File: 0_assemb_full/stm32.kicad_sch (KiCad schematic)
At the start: 15 parts, among them J4 Conn_01x02, J5 SPIConn_01x03, U25 STM32F091RCTx

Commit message: Updates to the filter system
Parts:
- added R33, R35, R36: 2k, symbol Device:R_US
- gave numbers to parts that had none: 7
- renumbered J4 to J3, J5 to J4, R62 to R34, U25 to U5
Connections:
- net ADC_BP: now also R35.1; no longer U5.9 (PC1)
- net ADC_HP: now also R36.1; no longer U5.10 (PC2)
- net ADC_LP: now also R33.2; no longer U5.8 (PC0)
- new net: R35.2, U5.9 (PC1)
- new net: R33.1, U5.8 (PC0)
- new net: R36.2, U5.10 (PC2)
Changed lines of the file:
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@@
     (stroke (width 0) (type default) (color 0 0 0 0))
   )
-  (wire (pts (xy 105.41 101.6) (xy 119.38 101.6))
+  (wire (pts (xy 105.41 109.22) (xy 109.22 109.22))
     (stroke (width 0) (type default) (color 0 0 0 0))
   )
@@
     (stroke (width 0) (type default) (color 0 0 0 0))
   )
-  (wire (pts (xy 105.41 96.52) (xy 119.38 96.52))
-    (stroke (width 0) (type default) (color 0 0 0 0))
-  )
   (wire (pts (xy 60.96 93.98) (xy 62.23 93.98))
     (stroke (width 0) (type default) (color 0 0 0 0))
@@
     (stroke (width 0) (type default) (color 0 0 0 0))
   )
+  (wire (pts (xy 109.22 96.52) (xy 119.38 96.52))
+    (stroke (width 0) (type default) (color 0 0 0 0))
+  )
   (wire (pts (xy 185.42 132.08) (xy 195.58 132.08))
     (stroke (width 0) (type default) (color 0 0 0 0))
@@
     (stroke (width 0) (type default) (color 0 0 0 0))
   )
-  (wire (pts (xy 105.41 99.06) (xy 119.38 99.06))
+  (wire (pts (xy 105.41 99.06) (xy 111.76 99.06))
     (stroke (width 0) (type default) (color 0 0 0 0))
   )
@@
   )
   (wire (pts (xy 45.72 73.66) (xy 45.72 74.93))
+    (stroke (width 0) (type default) (color 0 0 0 0))
+  )
+  (wire (pts (xy 109.22 101.6) (xy 119.38 101.6))
+    (stroke (width 0) (type default) (color 0 0 0 0))
+  )
+  (wire (pts (xy 105.41 88.9) (xy 109.22 88.9))
     (stroke (width 0) (type default) (color 0 0 0 0))
   )
@@
     )
   )
-  (global_label "ADC_HP" (shape input) (at 105.41 101.6 180) (fields_autoplaced)
+  (global_label "ADC_HP" (shape input) (at 105.41 109.22 180) (fields_autoplaced)
     (effects (font (size 1.27 1.27)) (justify right))
-    (property "Intersheet References" "${INTERSHEET_REFS}" (id 0) (at 95.8002 101.5206 0)
+    (property "Intersheet References" "${INTERSHEET_REFS}" (id 0) (at 95.8002 109.1406 0)
       (effects (font (size 1.27 1.27)) (justify right) hide)
     )
   )
-  (global_label "ADC_LP" (shape input) (at 105.41 96.52 180) (fields_autoplaced)
+  (global_label "ADC_LP" (shape input) (at 105.41 88.9 180) (fields_autoplaced)
     (effects (font (size 1.27 1.27)) (justify right))
-    (property "Intersheet References" "${INTERSHEET_REFS}" (id 0) (at 96.1026 96.4406 0)
+    (property "Intersheet References" "${INTERSHEET_REFS}" (id 0) (at 96.1026 88.8206 0)
       (effects (font (size 1.27 1.27)) (justify right) hide)
     )
@@
   (symbol (lib_id "Connector_Generic:Conn_01x03") (at 200.66 129.54 0) (unit 1)
     (in_bom yes) (on_board yes) (fields_autoplaced)
-    (property "Reference" "J5" (id 0) (at 203.2 128.2699 0)
+    (property "Reference" "J4" (id 0) (at 203.2 128.2699 0)
       (effects (font (size 1.27 1.27)) (justify left))
     )
@@
   (symbol (lib_id "Device:C") (at 31.75 25.4 0) (unit 1)
     (in_bom yes) (on_board yes) (fields_autoplaced)
-    (property "Reference" "C?" (id 0) (at 35.56 24.1299 0)
+    (property "Reference" "C13" (id 0) (at 35.56 24.1299 0)
       (effects (font (size 1.27 1.27)) (justify left))
     )
@@
   (symbol (lib_id "Device:R_US") (at 66.04 93.98 90) (unit 1)
     (in_bom yes) (on_board yes) (fields_autoplaced)
-    (property "Reference" "R62" (id 0) (at 66.04 87.63 90))
+    (property "Reference" "R34" (id 0) (at 66.04 87.63 90))
     (property "Value" "100K" (id 1) (at 66.04 90.17 90))
     (property "Footprint" "" (id 2) (at 66.294 92.964 90)
@@
   (symbol (lib_id "power:GND") (at 20.32 99.06 0) (unit 1)
     (in_bom yes) (on_board yes) (fields_autoplaced)
-    (property "Reference" "#PWR032" (id 0) (at 20.32 105.41 0)
+    (property "Reference" "#PWR015" (id 0) (at 20.32 105.41 0)
       (effects (font (size 1.27 1.27)) hide)
     )
@@
   (symbol (lib_id "Connector_Generic:Conn_01x02") (at 36.83 91.44 0) (unit 1)
     (in_bom yes) (on_board yes) (fields_autoplaced)
-    (property "Reference" "J4" (id 0) (at 39.37 91.4399 0)
+    (property "Reference" "J3" (id 0) (at 39.37 91.4399 0)
       (effects (font (size 1.27 1.27)) (justify left))
     )
@@
   (symbol (lib_id "power:GND") (at 30.48 95.25 0) (unit 1)
     (in_bom yes) (on_board yes) (fields_autoplaced)
-    (property "Reference" "#PWR030" (id 0) (at 30.48 101.6 0)
+    (property "Reference" "#PWR013" (id 0) (at 30.48 101.6 0)
       (effects (font (size 1.27 1.27)) hide)
     )
@@
   (symbol (lib_id "Device:C") (at 59.69 69.85 0) (unit 1)
     (in_bom yes) (on_board yes) (fields_autoplaced)
-    (property "Reference" "C?" (id 0) (at 63.5 68.5799 0)
+    (property "Reference" "C20" (id 0) (at 63.5 68.5799 0)
       (effects (font (size 1.27 1.27)) (justify left))
     )
@@
   (symbol (lib_id "power:GND") (at 60.96 95.25 0) (unit 1)
     (in_bom yes) (on_board yes) (fields_autoplaced)
-    (property "Reference" "#PWR031" (id 0) (at 60.96 101.6 0)
+    (property "Reference" "#PWR014" (id 0) (at 60.96 101.6 0)
       (effects (font (size 1.27 1.27)) hide)
     )
@@
   (symbol (lib_id "Device:C") (at 45.72 45.72 0) (unit 1)
     (in_bom yes) (on_board yes) (fields_autoplaced)
-    (property "Reference" "C?" (id 0) (at 49.53 44.4499 0)
+    (property "Reference" "C18" (id 0) (at 49.53 44.4499 0)
       (effects (font (size 1.27 1.27)) (justify left))
     )
@@
   (symbol (lib_id "Device:C") (at 45.72 69.85 0) (unit 1)
     (in_bom yes) (on_board yes) (fields_autoplaced)
-    (property "Reference" "C?" (id 0) (at 49.53 68.5799 0)
+    (property "Reference" "C19" (id 0) (at 49.53 68.5799 0)
       (effects (font (size 1.27 1.27)) (justify left))
     )
@@
   (symbol (lib_id "power:GND") (at 52.07 76.2 0) (unit 1)
     (in_bom yes) (on_board yes) (fields_autoplaced)
-    (property "Reference" "#PWR029" (id 0) (at 52.07 82.55 0)
+    (property "Reference" "#PWR012" (id 0) (at 52.07 82.55 0)
       (effects (font (size 1.27 1.27)) hide)
     )
@@
     (pin "1")
   )
+  (symbol (lib_id "Device:R_US") (at 115.57 99.06 90) (unit 1)
+    (in_bom yes) (on_board yes) (fields_autoplaced)
+    (property "Reference" "R35" (id 0) (at 115.57 92.71 90))
+    (property "Value" "2k" (id 1) (at 115.57 95.25 90))
+    (property "Footprint" "" (id 2) (at 115.824 98.044 90)
+      (effects (font (size 1.27 1.27)) hide)
+    )
+    (property "Datasheet" "~" (id 3) (at 115.57 99.06 0)
+      (effects (font (size 1.27 1.27)) hide)
+    )
+    (pin "1")
+    (pin "2")
+  )
   (symbol (lib_id "power:GND") (at 52.07 31.75 0) (unit 1)
     (in_bom yes) (on_board yes) (fields_autoplaced)
-    (property "Reference" "#PWR027" (id 0) (at 52.07 38.1 0)
+    (property "Reference" "#PWR010" (id 0) (at 52.07 38.1 0)
       (effects (font (size 1.27 1.27)) hide)
     )
@@
     (pin "1")
   )
+  (symbol (lib_id "Device:R_US") (at 109.22 92.71 180) (unit 1)
+    (in_bom yes) (on_board yes) (fields_autoplaced)
+    (property "Reference" "R33" (id 0) (at 111.76 91.4399 0)
+      (effects (font (size 1.27 1.27)) (justify right))
+    )
+    (property "Value" "2k" (id 1) (at 111.76 93.9799 0)
+      (effects (font (size 1.27 1.27)) (justify right))
+    )
+    (property "Footprint" "" (id 2) (at 108.204 92.456 90)
+      (effects (font (size 1.27 1.27)) hide)
+    )
+    (property "Datasheet" "~" (id 3) (at 109.22 92.71 0)
+      (effects (font (size 1.27 1.27)) hide)
+    )
+    (pin "1")
+    (pin "2")
+  )
   (symbol (lib_id "power:GND") (at 38.1 52.07 0) (unit 1)
     (in_bom yes) (on_board yes) (fields_autoplaced)
-    (property "Reference" "#PWR028" (id 0) (at 38.1 58.42 0)
+    (property "Reference" "#PWR011" (id 0) (at 38.1 58.42 0)
       (effects (font (size 1.27 1.27)) hide)
     )
@@
   (symbol (lib_id "Device:R_US") (at 34.29 85.09 90) (unit 1)
     (in_bom yes) (on_board yes) (fields_autoplaced)
-    (property "Reference" "R?" (id 0) (at 34.29 78.74 90))
+    (property "Reference" "R32" (id 0) (at 34.29 78.74 90))
     (property "Value" "100K" (id 1) (at 34.29 81.28 90))
     (property "Footprint" "" (id 2) (at 34.544 84.074 90)
@@
     (pin "2")
   )
+  (symbol (lib_id "Device:R_US") (at 109.22 105.41 180) (unit 1)
+    (in_bom yes) (on_board yes) (fields_autoplaced)
+    (property "Reference" "R36" (id 0) (at 111.76 104.1399 0)
+      (effects (font (size 1.27 1.27)) (justify right))
+    )
+    (property "Value" "2k" (id 1) (at 111.76 106.6799 0)
+      (effects (font (size 1.27 1.27)) (justify right))
+    )
+    (property "Footprint" "" (id 2) (at 108.204 105.156 90)
+      (effects (font (size 1.27 1.27)) hide)
+    )
+    (property "Datasheet" "~" (id 3) (at 109.22 105.41 0)
+      (effects (font (size 1.27 1.27)) hide)
+    )
+    (pin "1")
+    (pin "2")
+  )
   (symbol (lib_id "power:GND") (at 134.62 142.24 0) (unit 1)
     (in_bom yes) (on_board yes) (fields_autoplaced)
-    (property "Reference" "#PWR033" (id 0) (at 134.62 148.59 0)
+    (property "Reference" "#PWR016" (id 0) (at 134.62 148.59 0)
       (effects (font (size 1.27 1.27)) hide)
     )
@@
   (symbol (lib_id "MCU_ST_STM32F0:STM32F091RCTx") (at 137.16 93.98 0) (unit 1)
     (in_bom yes) (on_board yes) (fields_autoplaced)
-    (property "Reference" "U25" (id 0) (at 141.7194 139.7 0)
+    (property "Reference" "U5" (id 0) (at 141.7194 139.7 0)
       (effects (font (size 1.27 1.27)) (justify left))
     )
@@
   (symbol (lib_id "Device:C") (at 73.66 25.4 0) (unit 1)
     (in_bom yes) (on_board yes) (fields_autoplaced)
-    (property "Reference" "C?" (id 0) (at 77.47 24.1299 0)
+    (property "Reference" "C16" (id 0) (at 77.47 24.1299 0)
       (effects (font (size 1.27 1.27)) (justify left))
     )
@@
   (symbol (lib_id "Device:C") (at 31.75 45.72 0) (unit 1)
     (in_bom yes) (on_board yes) (fields_autoplaced)
-    (property "Reference" "C?" (id 0) (at 35.56 44.4499 0)
-      (effects (font (size 1.27 1.27)) (justify left))
-    )
+    (property "Reference" "C17" (id 0) (at 35.56 44.4499 0)
+      (effects (font (size 1.27 1.27)) (justify left))
+    )

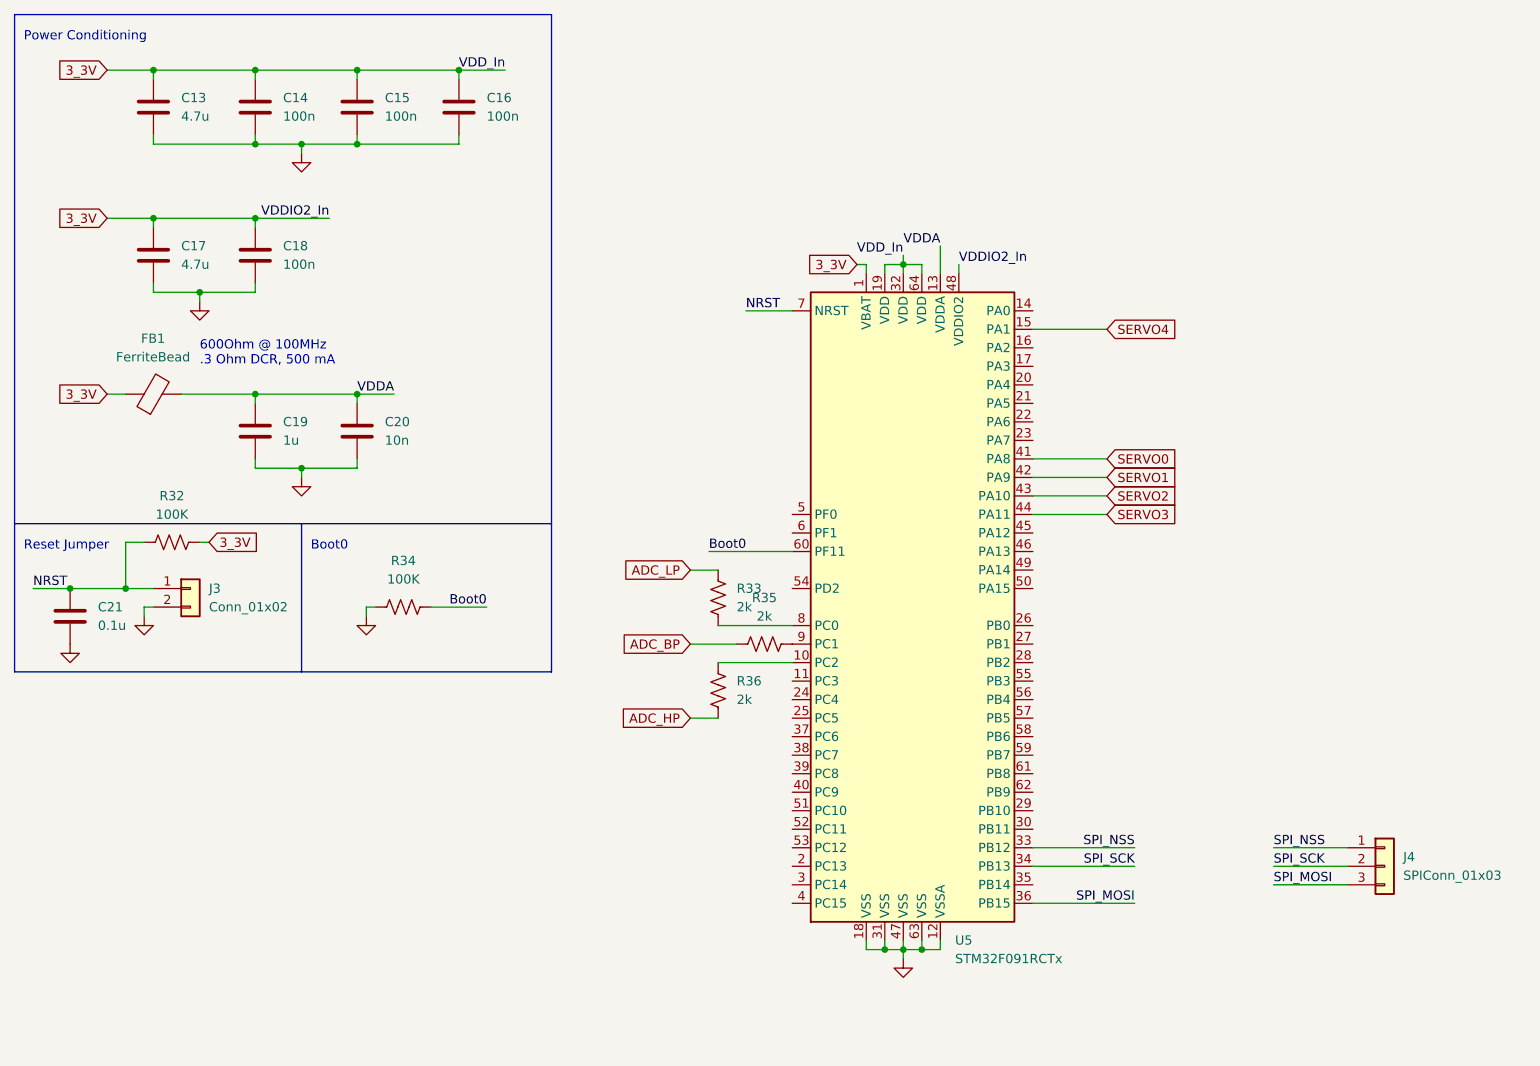
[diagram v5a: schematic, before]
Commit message: Added amplifier circuit and the programming header.
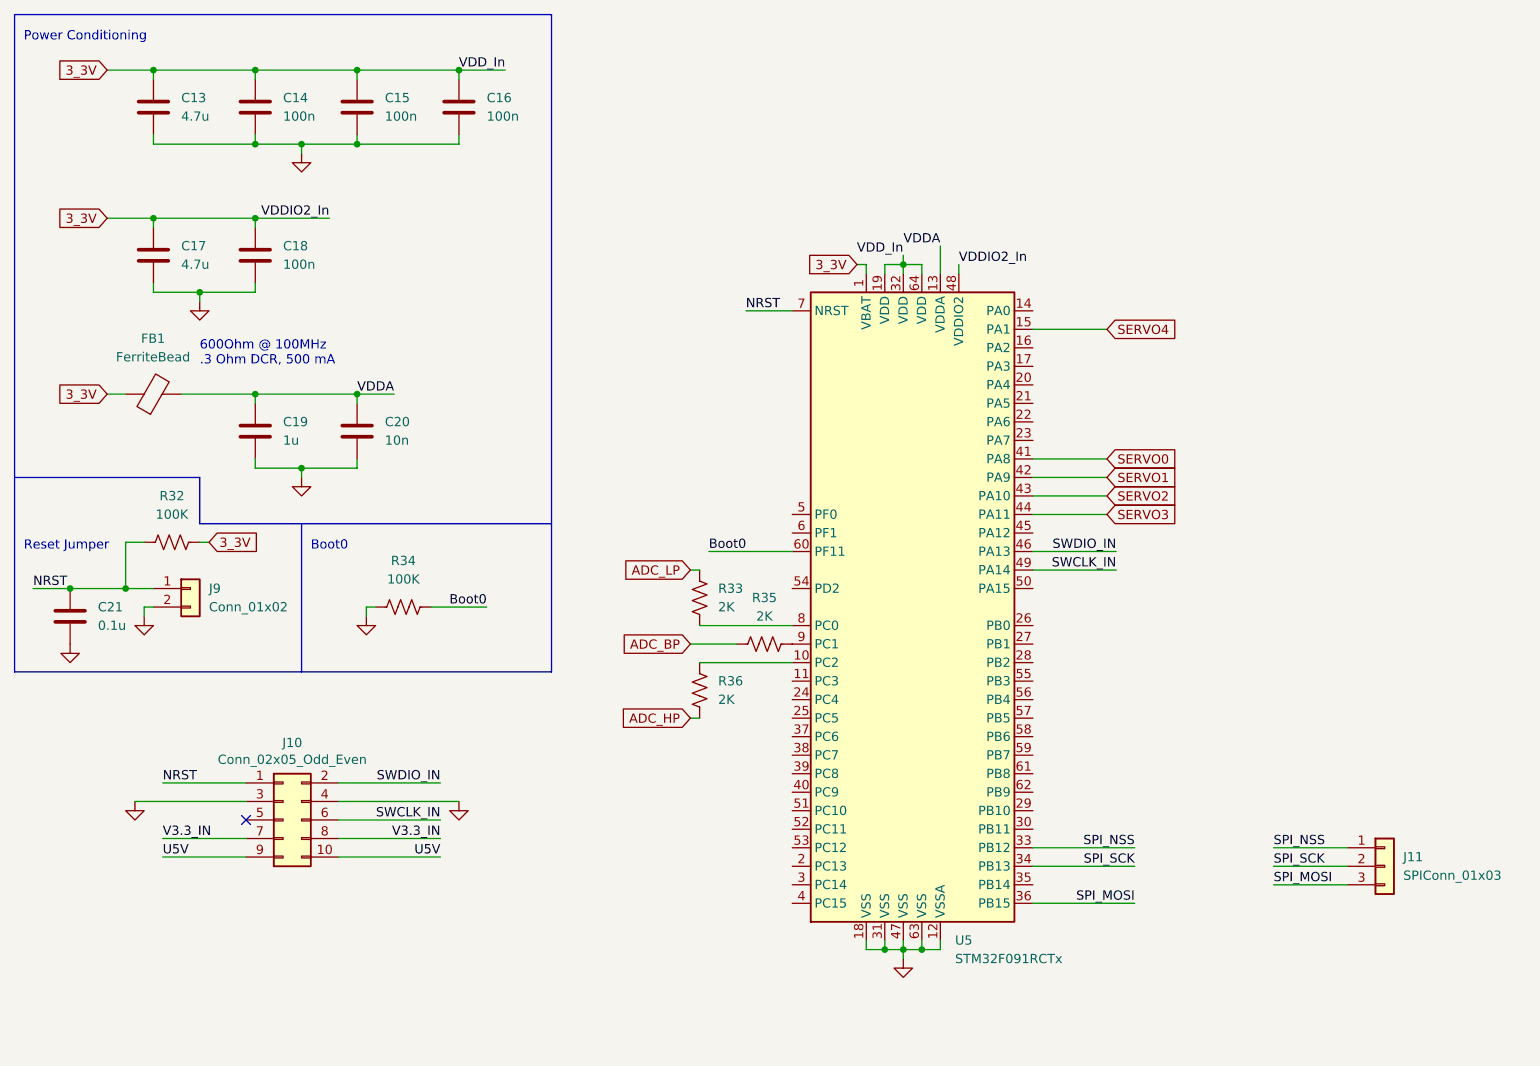
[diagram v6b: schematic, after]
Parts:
- added J10: Conn_02x05_Odd_Even, Connector_IDC:IDC-Header_2x05_P2.54mm_Vertical, symbol Connector_Generic:Conn_02x05_Odd_Even
- R33, R35, R36: value 2k -> 2K
- renumbered J4 to J11, J3 to J9
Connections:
- net GND: now also J10.3 (Pin_3), J10.4 (Pin_4)
- net NRST: now also J10.1 (Pin_1)
- net SWDIO_IN: now reaches U5.46 (PA13)
- net SWDIO_IN: now also J10.2 (Pin_2)
- net SWCLK_IN: now reaches U5.49 (PA14)
- net SWCLK_IN: now also J10.6 (Pin_6)
- new net U5V: J10.10 (Pin_10), J10.9 (Pin_9)
- new net V3.3_IN: J10.7 (Pin_7), J10.8 (Pin_8)
- no-connect marks 0 -> 1
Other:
- moved on the sheet: R33, R36
